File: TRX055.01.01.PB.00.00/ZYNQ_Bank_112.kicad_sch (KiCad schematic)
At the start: 20 parts, among them J6 Micro_SD_Card, U1 XC7Z015-1CLG485I, U12 USB3320C-EZK-TR, U14 W25Q128JVSIQ

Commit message: Update Layout
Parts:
- removed J6: Micro_SD_Card, Connector_Card:microSD_HC_Molex_47219-2001, symbol Connector:Micro_SD_Card
- removed R12, R14, R17, R18, R19, R20, R21, R22, R23, R24, R25, R26, R27, R28, R29: 33R, Resistor_SMD:R_0402_1005Metric, symbol PPA-Pasive:Res
- removed U1: XC7Z015-1CLG485I, CLG485XC7Z012S/XC7Z015_AMD, symbol XC7Z015-1CLG485C:XC7Z015-1CLG485I
- removed U10: ~, ppa-active:XQFN16, symbol ppa-ic-com:NVT4858HKZ
- removed U12: USB3320C-EZK-TR, Package_DFN_QFN:QFN-32-1EP_5x5mm_P0.5mm_EP3.3x3.3mm, symbol ppa-ic-com:USB3320C-EZK-TR
- removed U14: W25Q128JVSIQ, Package_SO:SOIC-8_5.23x5.23mm_P1.27mm, symbol Memory_Flash:W25Q128JVS
- added C100, C101, C102, C103, C104, C105, C106, C107, C88, C89, C90, C91, C92, C93, C94, C95, C96, C97, C98, C99: M1, Capacitor_SMD:C_0201_0603Metric, symbol PPA-Pasive:Cap
- added U1: XC7Z015-1CLG485I, CLG485XC7Z012S/XC7Z015_AMD, symbol XC7Z015-1CLG485C:XC7Z015-1CLG485I
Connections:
- new net: C97.2, U1.AB3 (MGTPTXN0_112)
- new net: C101.2, U1.AA5 (MGTPTXP2_112)
- new net: C96.2, U1.AA3 (MGTPTXP0_112)
- new net: C90.2, U1.AA7 (MGTPRXP0_112)
- new net: C92.2, U1.AA9 (MGTPRXP2_112)
- new net: C100.2, U1.AB5 (MGTPTXN2_112)
- new net: C91.2, U1.AB7 (MGTPRXN0_112)
- new net: C93.2, U1.AB9 (MGTPRXN2_112)
- new net: C105.2, U1.U5 (MGTREFCLK1P_112)
- new net: C104.2, U1.U9 (MGTREFCLK0P_112)
- new net: C107.2, U1.V5 (MGTREFCLK1N_112)
- new net: C106.2, U1.V9 (MGTREFCLK0N_112)
- new net: C103.2, U1.W2 (MGTPTXP3_112)
- new net: C99.2, U1.W4 (MGTPTXP1_112)
- new net: C94.2, U1.W6 (MGTPRXP3_112)
- new net: C88.2, U1.W8 (MGTPRXP1_112)
- new net: C102.2, U1.Y2 (MGTPTXN3_112)
- new net: C98.2, U1.Y4 (MGTPTXN1_112)
- new net: C95.2, U1.Y6 (MGTPRXN3_112)
- new net: C89.2, U1.Y8 (MGTPRXN1_112)
- new net GTP_REF_CLK0_N: C106.1
- new net GTP_REF_CLK0_P: C104.1
- new net GTP_REF_CLK1_N: C107.1
- new net GTP_REF_CLK1_P: C105.1
- new net GTP_RX0_N: C91.1
- new net GTP_RX0_P: C90.1
- new net GTP_RX1_N: C89.1
- new net GTP_RX1_P: C88.1
- new net GTP_RX2_N: C93.1
- new net GTP_RX2_P: C92.1
- new net GTP_RX3_N: C95.1
- new net GTP_RX3_P: C94.1
- new net GTP_TX0_N: C97.1
- new net GTP_TX0_P: C96.1
- new net GTP_TX1_N: C98.1
- new net GTP_TX1_P: C99.1
- new net GTP_TX2_N: C100.1
- new net GTP_TX2_P: C101.1
- new net GTP_TX3_N: C102.1
- new net GTP_TX3_P: C103.1

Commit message: +ETH +USB +Connectors
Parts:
- C100, C101, C102, C103, C104, C105, C106, C107, C88, C89, C90, C91, C92, C93, C94, C95, C96, C97, C98, C99: footprint Capacitor_SMD:C_0201_0603Metric -> Capacitor_SMD:C_0402_1005Metric
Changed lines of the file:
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@@
 			)
 		)
-		(property "Footprint" "Capacitor_SMD:C_0201_0603Metric"
+		(property "Footprint" "Capacitor_SMD:C_0402_1005Metric"
 			(at 186.69 90.17 0)
 			(effects
@@
 			)
 		)
-		(property "Footprint" "Capacitor_SMD:C_0201_0603Metric"
+		(property "Footprint" "Capacitor_SMD:C_0402_1005Metric"
 			(at 201.93 102.87 0)
 			(effects
@@
 			)
 		)
-		(property "Footprint" "Capacitor_SMD:C_0201_0603Metric"
+		(property "Footprint" "Capacitor_SMD:C_0402_1005Metric"
 			(at 201.93 110.49 0)
 			(effects
@@
 			)
 		)
-		(property "Footprint" "Capacitor_SMD:C_0201_0603Metric"
+		(property "Footprint" "Capacitor_SMD:C_0402_1005Metric"
 			(at 86.36 110.49 0)
 			(effects
@@
 			)
 		)
-		(property "Footprint" "Capacitor_SMD:C_0201_0603Metric"
+		(property "Footprint" "Capacitor_SMD:C_0402_1005Metric"
 			(at 186.69 97.79 0)
 			(effects
@@
 			)
 		)
-		(property "Footprint" "Capacitor_SMD:C_0201_0603Metric"
+		(property "Footprint" "Capacitor_SMD:C_0402_1005Metric"
 			(at 86.36 87.63 0)
 			(effects
@@
 			)
 		)
-		(property "Footprint" "Capacitor_SMD:C_0201_0603Metric"
+		(property "Footprint" "Capacitor_SMD:C_0402_1005Metric"
 			(at 201.93 87.63 0)
 			(effects
@@
 			)
 		)
-		(property "Footprint" "Capacitor_SMD:C_0201_0603Metric"
+		(property "Footprint" "Capacitor_SMD:C_0402_1005Metric"
 			(at 105.41 97.79 0)
 			(effects
@@
 			)
 		)
-		(property "Footprint" "Capacitor_SMD:C_0201_0603Metric"
+		(property "Footprint" "Capacitor_SMD:C_0402_1005Metric"
 			(at 201.93 95.25 0)
 			(effects
@@
 			)
 		)
-		(property "Footprint" "Capacitor_SMD:C_0201_0603Metric"
+		(property "Footprint" "Capacitor_SMD:C_0402_1005Metric"
 			(at 186.69 105.41 0)
 			(effects
@@
 			)
 		)
-		(property "Footprint" "Capacitor_SMD:C_0201_0603Metric"
+		(property "Footprint" "Capacitor_SMD:C_0402_1005Metric"
 			(at 105.41 113.03 0)
 			(effects
@@
 			)
 		)
-		(property "Footprint" "Capacitor_SMD:C_0201_0603Metric"
+		(property "Footprint" "Capacitor_SMD:C_0402_1005Metric"
 			(at 86.36 127 0)
 			(effects
@@
 			)
 		)
-		(property "Footprint" "Capacitor_SMD:C_0201_0603Metric"
+		(property "Footprint" "Capacitor_SMD:C_0402_1005Metric"
 			(at 105.41 105.41 0)
 			(effects
@@
 			)
 		)
-		(property "Footprint" "Capacitor_SMD:C_0201_0603Metric"
+		(property "Footprint" "Capacitor_SMD:C_0402_1005Metric"
 			(at 105.41 90.17 0)
 			(effects
@@
 			)
 		)
-		(property "Footprint" "Capacitor_SMD:C_0201_0603Metric"
+		(property "Footprint" "Capacitor_SMD:C_0402_1005Metric"
 			(at 86.36 95.25 0)
 			(effects
@@
 			)
 		)
-		(property "Footprint" "Capacitor_SMD:C_0201_0603Metric"
+		(property "Footprint" "Capacitor_SMD:C_0402_1005Metric"
 			(at 86.36 120.65 0)
 			(effects
@@
 			)
 		)
-		(property "Footprint" "Capacitor_SMD:C_0201_0603Metric"
+		(property "Footprint" "Capacitor_SMD:C_0402_1005Metric"
 			(at 105.41 129.54 0)
 			(effects
@@
 			)
 		)
-		(property "Footprint" "Capacitor_SMD:C_0201_0603Metric"
+		(property "Footprint" "Capacitor_SMD:C_0402_1005Metric"
 			(at 105.41 123.19 0)
 			(effects
@@
 			)
 		)
-		(property "Footprint" "Capacitor_SMD:C_0201_0603Metric"
+		(property "Footprint" "Capacitor_SMD:C_0402_1005Metric"
 			(at 186.69 113.03 0)
 			(effects
@@
 			)
 		)
-		(property "Footprint" "Capacitor_SMD:C_0201_0603Metric"
+		(property "Footprint" "Capacitor_SMD:C_0402_1005Metric"
 			(at 86.36 102.87 0)
 			(effects

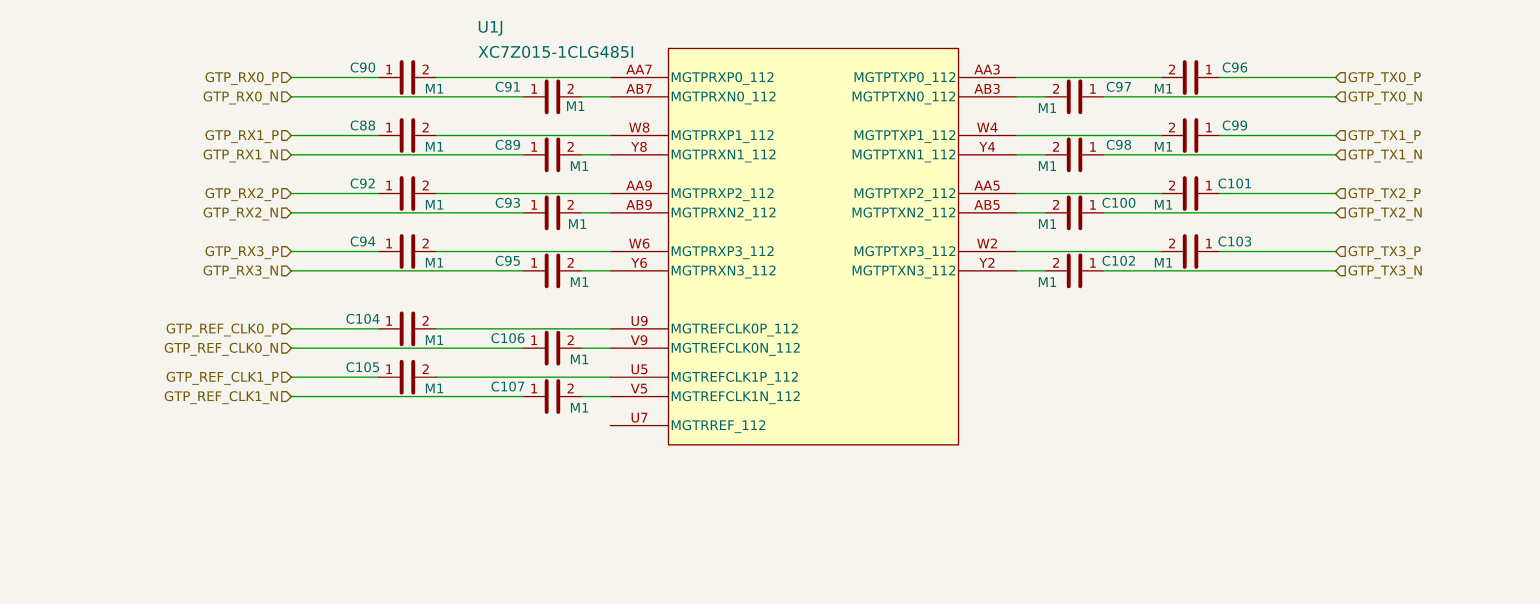
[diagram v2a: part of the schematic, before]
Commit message: + add clocks + add PSU
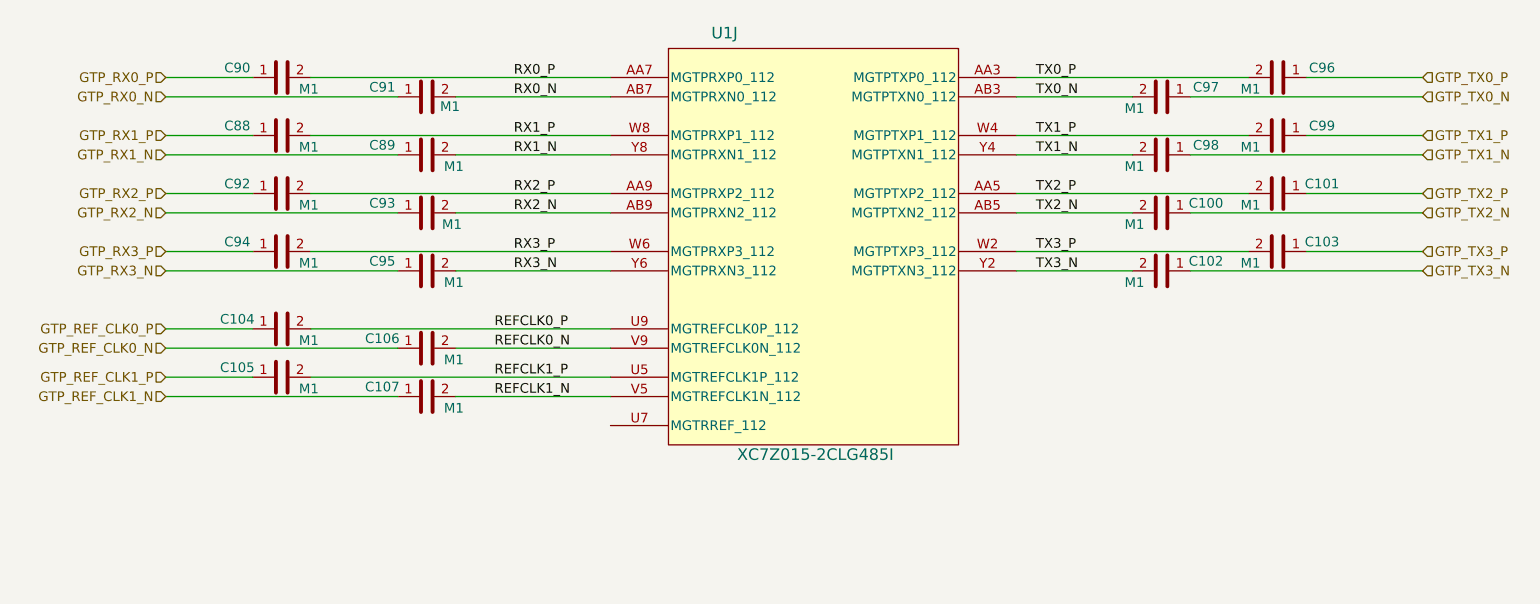
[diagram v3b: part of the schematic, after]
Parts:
- C100, C101, C102, C103, C104, C105, C106, C107, C88, C89, C90, C91, C92, C93, C94, C95, C96, C97, C98, C99: footprint Capacitor_SMD:C_0402_1005Metric -> Capacitor_SMD:C_0201_0603Metric; JLCPCB Part # (none) -> C1581
- U1: value XC7Z015-1CLG485I -> XC7Z015-2CLG485I; JLCPCB Part # C1522056 -> C1522056
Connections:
- net TX0_N: now reaches C97.2, U1.AB3 (MGTPTXN0_112)
- net TX2_P: now reaches C101.2, U1.AA5 (MGTPTXP2_112)
- net TX0_P: now reaches C96.2, U1.AA3 (MGTPTXP0_112)
- net RX0_P: now reaches C90.2, U1.AA7 (MGTPRXP0_112)
- net RX2_P: now reaches C92.2, U1.AA9 (MGTPRXP2_112)
- net TX2_N: now reaches C100.2, U1.AB5 (MGTPTXN2_112)
- net RX0_N: now reaches C91.2, U1.AB7 (MGTPRXN0_112)
- net RX2_N: now reaches C93.2, U1.AB9 (MGTPRXN2_112)
- net REFCLK1_P: now reaches C105.2, U1.U5 (MGTREFCLK1P_112)
- net REFCLK0_P: now reaches C104.2, U1.U9 (MGTREFCLK0P_112)
- net REFCLK1_N: now reaches C107.2, U1.V5 (MGTREFCLK1N_112)
- net REFCLK0_N: now reaches C106.2, U1.V9 (MGTREFCLK0N_112)
- net TX3_P: now reaches C103.2, U1.W2 (MGTPTXP3_112)
- net TX1_P: now reaches C99.2, U1.W4 (MGTPTXP1_112)
- net RX3_P: now reaches C94.2, U1.W6 (MGTPRXP3_112)
- net RX1_P: now reaches C88.2, U1.W8 (MGTPRXP1_112)
- net TX3_N: now reaches C102.2, U1.Y2 (MGTPTXN3_112)
- net TX1_N: now reaches C98.2, U1.Y4 (MGTPTXN1_112)
- net RX3_N: now reaches C95.2, U1.Y6 (MGTPRXN3_112)
- net RX1_N: now reaches C89.2, U1.Y8 (MGTPRXN1_112)
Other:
- moved on the sheet: C100, C101, C102, C103, C104, C105, C106, C107, C88, C89, C90, C91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

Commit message: V0.1 - production, added brig-up comments
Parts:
- added R152: 500, Resistor_SMD:R_0402_1005Metric, symbol PPA-Pasive:Res
- U1: footprint CLG485XC7Z012S/XC7Z015_AMD -> XC7Z015:CLG485XC7Z012S&slash_XC7Z015_AMD
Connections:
- net at U1.U7 (MGTRREF_112): now also R152.1
- new net GND: R152.2
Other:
- company: (none) -> Tronex s.r.o. / Tronex Group USA LLC
- title: (none) -> TRNX SDR Carrier board
